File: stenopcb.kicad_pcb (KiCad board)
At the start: 2 copper layers, 100.3 x 95.2 mm, 83 parts, among them K1 MAIN_RIGHT_TO_VOWELS_RIGHT, K2 MAIN_LEFT_TO_VOWELS_LEFT, K3 VOWELS_RIGHT_IN, K4 VOWELS_LEFT_IN, P1 MAIN_RIGHT_IN, P2 MAIN_RIGHT_TO_MAIN_LEFT, P3 MAIN_LEFT_IN, SW1 SPST, SW10 SPST, SW11 SPST, SW12 SPST, SW13 SPST, SW14 SPST, SW15 SPST, SW16 SPST, SW17 SPST, SW18 SPST, SW19 SPST, SW2 SPST, SW20 SPST, SW21 SPST, SW22 SPST, SW23 SPST, SW24 SPST, SW25 SPST, SW26 SPST, SW27 SPST, SW28 SPST, SW29 SPST, SW3 SPST, SW30 SPST, SW4 SPST, SW5 SPST, SW6 SPST, SW7 SPST, SW8 SPST, SW9 SPST

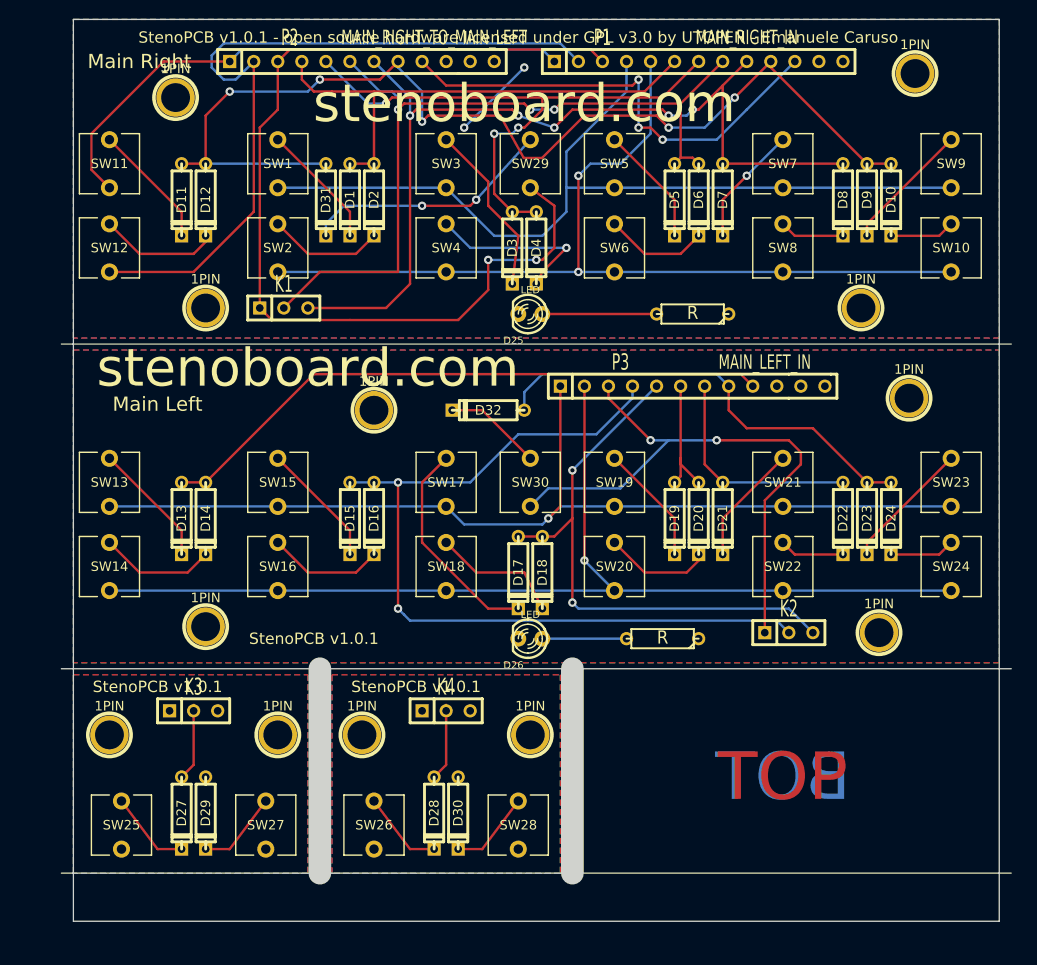
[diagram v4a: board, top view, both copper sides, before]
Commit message: fix silkscreen issues and user text tweaks
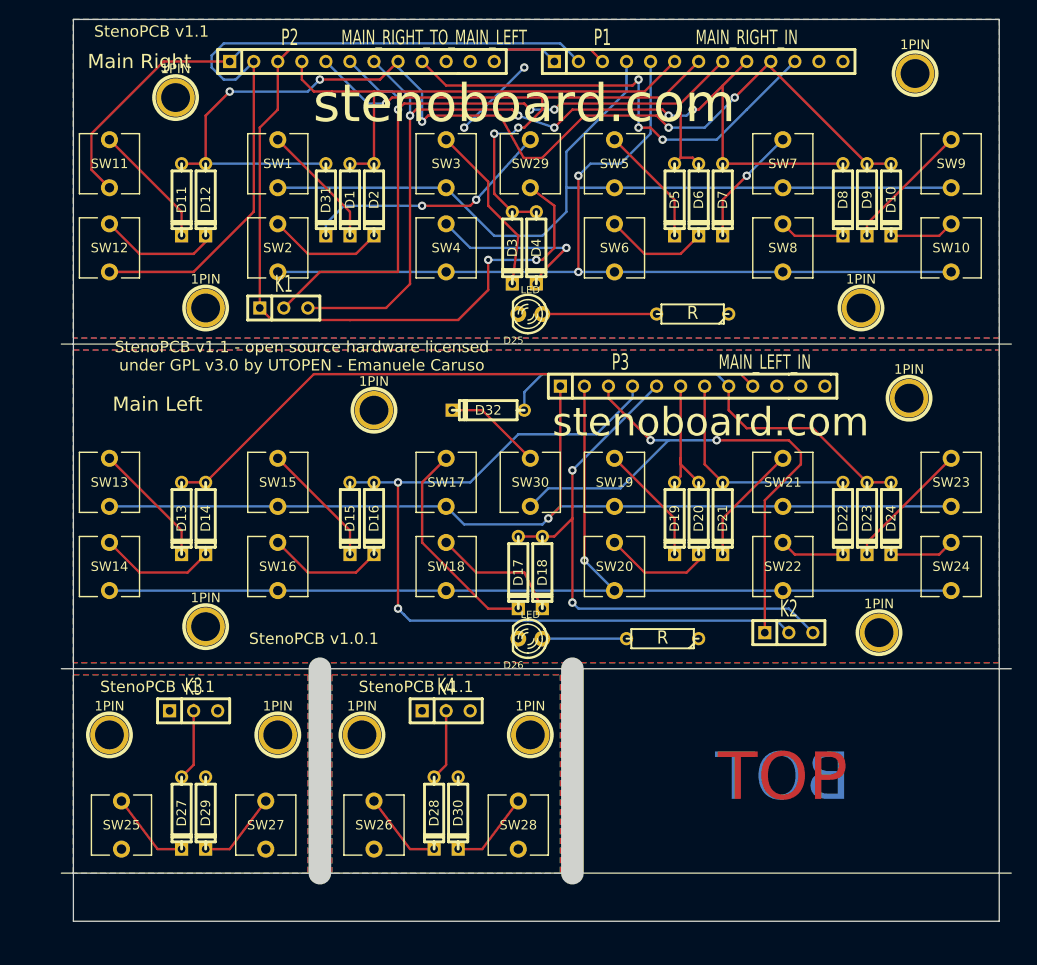
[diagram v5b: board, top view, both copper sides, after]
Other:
- board text added: "StenoPCB v1.1"
- board text added: "StenoPCB v1.1 - open source hardware licensed under GPL v3.0 by UTOPEN - Emanuele Caruso"
- board text removed: "StenoPCB v1.0.1 - open source hardware licensed under GPL v3.0 by UTOPEN - Emanuele Caruso"
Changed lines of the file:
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@@
     (area 91.694999 45.410001 231.440714 177.325)
     (thickness 1.6)
-    (drawings 48)
+    (drawings 49)
     (tracks 346)
     (zones 0)
@@
     (22 B.Mask user)
     (23 F.Mask user)
-    (24 Dwgs.User user hide)
+    (24 Dwgs.User user)
     (25 Cmts.User user)
     (26 Eco1.User user)
@@
     )
   )
+  (gr_text stenoboard.com (at 178.435 104.775) (layer F.SilkS)
+    (effects (font (size 3 3) (thickness 0.3)))
+  )
+  (gr_text "StenoPCB v1.1" (at 119.38 63.5) (layer F.SilkS)
+    (effects (font (size 1.2 1.2) (thickness 0.3)))
+  )
   (gr_line (start 163.83 130.81) (end 163.83 152.4) (angle 90) (layer Edge.Cuts) (width 2.4))
   (gr_line (start 137.16 130.81) (end 137.16 152.4) (angle 90) (layer Edge.Cuts) (width 2.4))
@@
     (effects (font (size 5 5) (thickness 0.3)))
   )
-  (gr_text "StenoPCB v1.0.1" (at 120.015 132.715) (layer F.SilkS)
+  (gr_text "StenoPCB v1.1" (at 120.015 132.715) (layer F.SilkS)
     (effects (font (size 1.2 1.2) (thickness 0.3)))
   )
-  (gr_text "StenoPCB v1.0.1" (at 147.32 132.715) (layer F.SilkS)
+  (gr_text "StenoPCB v1.1" (at 147.32 132.715) (layer F.SilkS)
     (effects (font (size 1.2 1.2) (thickness 0.3)))
   )
@@
     (effects (font (size 1.2 1.2) (thickness 0.3)))
   )
-  (gr_text "StenoPCB v1.0.1 - open source hardware licensed under GPL v3.0 by UTOPEN - Emanuele Caruso" (at 158.115 64.135) (layer F.SilkS)
+  (gr_text "StenoPCB v1.1 - open source hardware licensed\nunder GPL v3.0 by UTOPEN - Emanuele Caruso" (at 135.255 97.79) (layer F.SilkS)
     (effects (font (size 1.2 1.2) (thickness 0.3)))
-  )
-  (gr_text stenoboard.com (at 135.89 99.06) (layer F.SilkS)
-    (effects (font (size 4 4) (thickness 0.3)))
   )
   (gr_text stenoboard.com (at 158.75 71.12) (layer F.SilkS)
     (effects (font (size 4 4) (thickness 0.3)))
   )
-  (gr_text Routing (at 167.64 156.21) (layer Dwgs.User)
+  (gr_text Routing (at 163.83 158.115 90) (layer Dwgs.User)
     (effects (font (size 1.5 1.5) (thickness 0.3)))
   )
-  (gr_text Routing (at 140.97 156.21) (layer Dwgs.User)
+  (gr_text Routing (at 137.795 158.115 90) (layer Dwgs.User)
     (effects (font (size 1.5 1.5) (thickness 0.3)))
   )

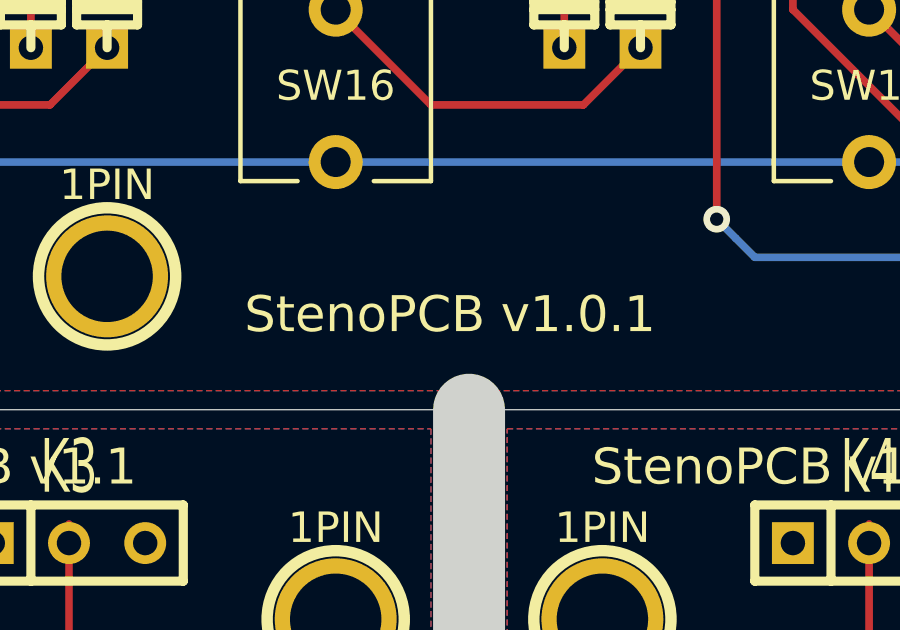
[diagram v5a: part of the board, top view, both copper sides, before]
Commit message: fixed minor silkscreen text issue
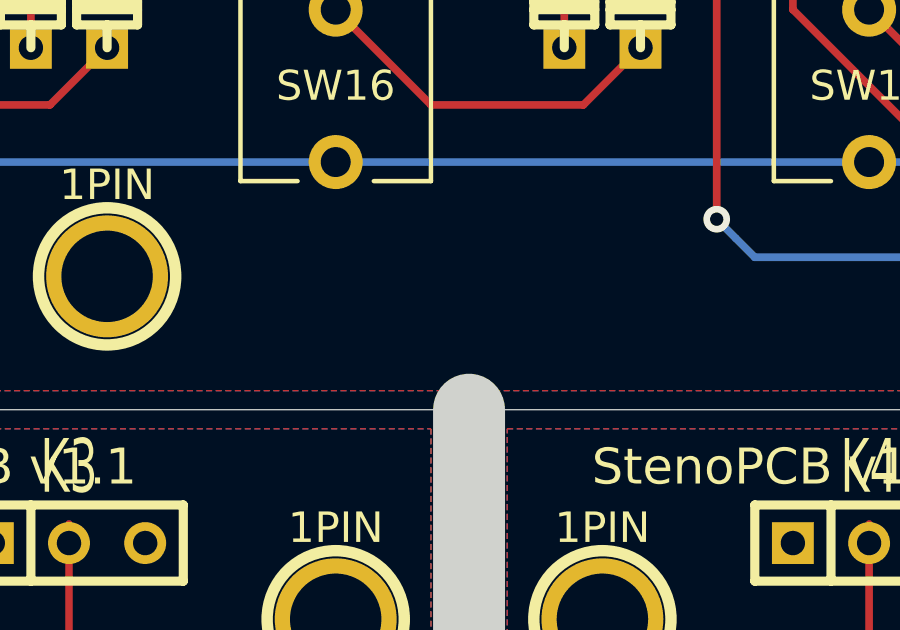
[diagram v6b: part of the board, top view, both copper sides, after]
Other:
- board text removed: "StenoPCB v1.0.1"
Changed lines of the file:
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@@
     (area 91.694999 45.410001 231.440714 177.325)
     (thickness 1.6)
-    (drawings 49)
+    (drawings 48)
     (tracks 346)
     (zones 0)
@@
     (effects (font (size 1.2 1.2) (thickness 0.3)))
   )
-  (gr_text "StenoPCB v1.0.1" (at 136.525 127.635) (layer F.SilkS)
-    (effects (font (size 1.2 1.2) (thickness 0.3)))
-  )
